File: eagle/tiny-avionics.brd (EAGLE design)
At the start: 65.8 x 25.4 mm, 61 parts, among them J1 USB-MICROB, J3 JST-PH-2-SMT-RA, U1 LP5907, U2 M25PX16, U3 LSM6DS3, U4 BQ21040, U5 LTC1998, U6 ATMEGA32U4-AU, X1 8MHz

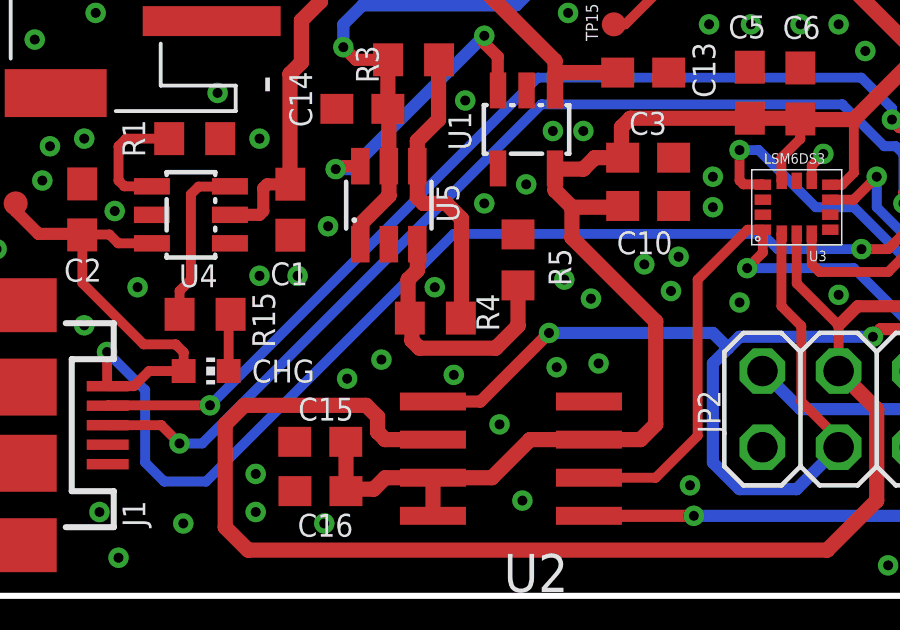
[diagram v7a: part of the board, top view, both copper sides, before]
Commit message: Added thermistor to bottom of board
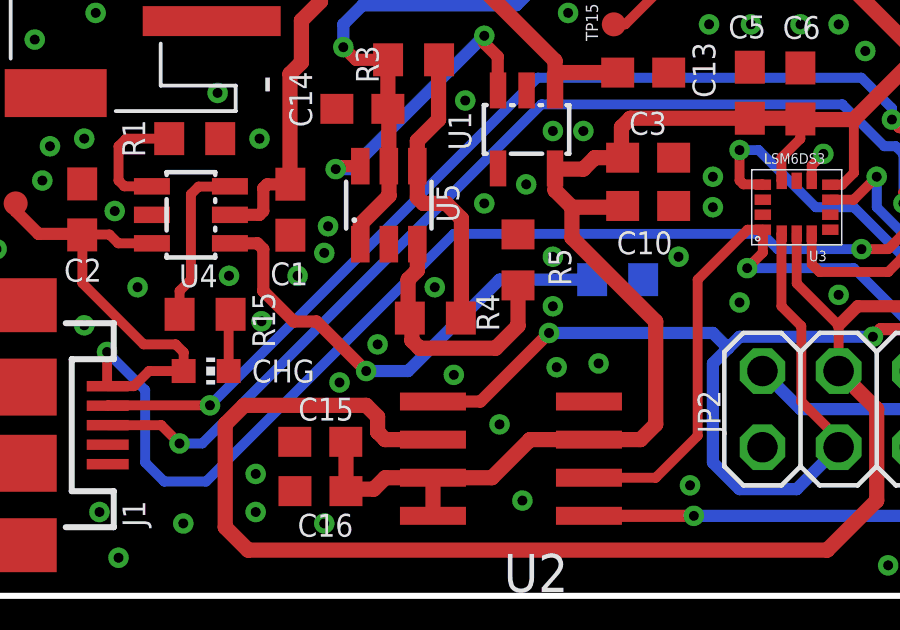
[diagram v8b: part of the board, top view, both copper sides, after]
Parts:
- added U$1: THERMISTOR-SMD0603, tinyav-lib:R0603
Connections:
- new net N$9: U$1.1, U4.1
- net GND: now also U$1.2
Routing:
- net N$9: track 0.00 -> 15.9 mm, vias 0 -> 1
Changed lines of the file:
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@@
 <attribute name="VALUE" x="22.225" y="12.7" size="1.27" layer="27"/>
 </element>
+<element name="U$1" library="tinyav-lib" package="R0603" value="THERMISTOR-SMD0603" x="21.844" y="10.541" rot="MR180"/>
 </elements>
 <signals>
@@
 <via x="12.065" y="2.413" extent="1-16" drill="0.3302"/>
 <via x="5.842" y="10.287" extent="1-16" drill="0.3302"/>
-<via x="9.906" y="10.668" extent="1-16" drill="0.3302"/>
+<via x="8.89" y="10.668" extent="1-16" drill="0.3302"/>
 <via x="12.192" y="12.319" extent="1-16" drill="0.3302"/>
 <via x="9.906" y="15.24" extent="1-16" drill="0.3302"/>
@@
 <via x="25.019" y="12.954" extent="1-16" drill="0.3302"/>
 <via x="25.019" y="13.97" extent="1-16" drill="0.3302"/>
-<via x="23.622" y="10.16" extent="1-16" drill="0.3302"/>
-<via x="22.733" y="11.049" extent="1-16" drill="0.3302"/>
 <via x="23.876" y="11.303" extent="1-16" drill="0.3302"/>
-<via x="20.955" y="9.906" extent="1-16" drill="0.3302"/>
-<via x="20.066" y="10.541" extent="1-16" drill="0.3302"/>
+<via x="19.685" y="9.652" extent="1-16" drill="0.3302"/>
+<via x="19.685" y="11.303" extent="1-16" drill="0.3302"/>
 <via x="18.796" y="13.716" extent="1-16" drill="0.3302"/>
 <via x="20.701" y="15.494" extent="1-16" drill="0.3302"/>
@@
 <via x="43.18" y="5.207" extent="1-16" drill="0.3302"/>
 <via x="40.386" y="4.318" extent="1-16" drill="0.3302"/>
-<via x="12.827" y="7.239" extent="1-16" drill="0.3302"/>
+<via x="13.843" y="8.382" extent="1-16" drill="0.3302"/>
 <via x="17.907" y="5.715" extent="1-16" drill="0.3302"/>
 <via x="18.669" y="3.175" extent="1-16" drill="0.3302"/>
@@
 <via x="5.08" y="12.827" extent="1-16" drill="0.3302"/>
 <via x="11.176" y="10.668" extent="1-16" drill="0.3302"/>
-<via x="13.97" y="7.874" extent="1-16" drill="0.3302"/>
+<via x="12.065" y="11.43" extent="1-16" drill="0.3302"/>
 <via x="16.383" y="7.366" extent="1-16" drill="0.3302"/>
 <via x="19.812" y="7.62" extent="1-16" drill="0.3302"/>
@@
 <via x="4.064" y="9.017" extent="1-16" drill="0.3302"/>
 <via x="48.514" y="7.62" extent="1-16" drill="0.3302"/>
-<wire x1="26.683" y1="13.204" x2="27.813" y2="13.834" width="0" layer="19" extent="1-1"/>
+<contactref element="U$1" pad="2"/>
+<via x="12.573" y="7.112" extent="1-16" drill="0.3302" diameter="0.6858"/>
+<via x="9.973" y="9.151" extent="1-16" drill="0.3302" diameter="0.6858"/>
+<wire x1="27.813" y1="13.834" x2="26.683" y2="13.204" width="0" layer="19" extent="1-1"/>
 </signal>
 <signal name="CLK">
@@
 <wire x1="43.815" y1="6.951" x2="43.764" y2="6.9" width="0.3302" layer="1"/>
 </signal>
+<signal name="N$9">
+<contactref element="U4" pad="1"/>
+<contactref element="U$1" pad="1"/>
+<wire x1="8.92" y1="11.75" x2="9.84" y2="11.75" width="0.4064" layer="1"/>
+<wire x1="9.84" y1="11.75" x2="10.033" y2="11.557" width="0.4064" layer="1"/>
+<wire x1="10.033" y1="11.557" x2="10.033" y2="10.16" width="0.4064" layer="1"/>
+<wire x1="10.033" y1="10.16" x2="11.049" y2="9.144" width="0.4064" layer="1"/>
+<wire x1="11.049" y1="9.144" x2="11.811" y2="9.144" width="0.4064" layer="1"/>
+<wire x1="11.811" y1="9.144" x2="13.462" y2="7.493" width="0.4064" layer="1"/>
+<via x="13.462" y="7.493" extent="1-16" drill="0.3302" diameter="0.6858"/>
+<wire x1="13.462" y1="7.493" x2="14.859" y2="7.493" width="0.4064" layer="16"/>
+<wire x1="14.859" y1="7.493" x2="17.907" y2="10.541" width="0.4064" layer="16"/>
+<wire x1="17.907" y1="10.541" x2="20.994" y2="10.541" width="0.4064" layer="16"/>
+</signal>
 </signals>
